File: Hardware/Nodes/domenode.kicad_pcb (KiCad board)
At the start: 2 copper layers, 100 x 65 mm, 9 parts, among them J10 CAN_BOARD, J12 RGB_SHIELD, J13 RGB_SHIELD, J15 CAN_IN, J16 CAN_OUT, U1 MINI-360, U2 AMS1117-3.3, U4 SN65HVD230, U5 ESP32-WROOM

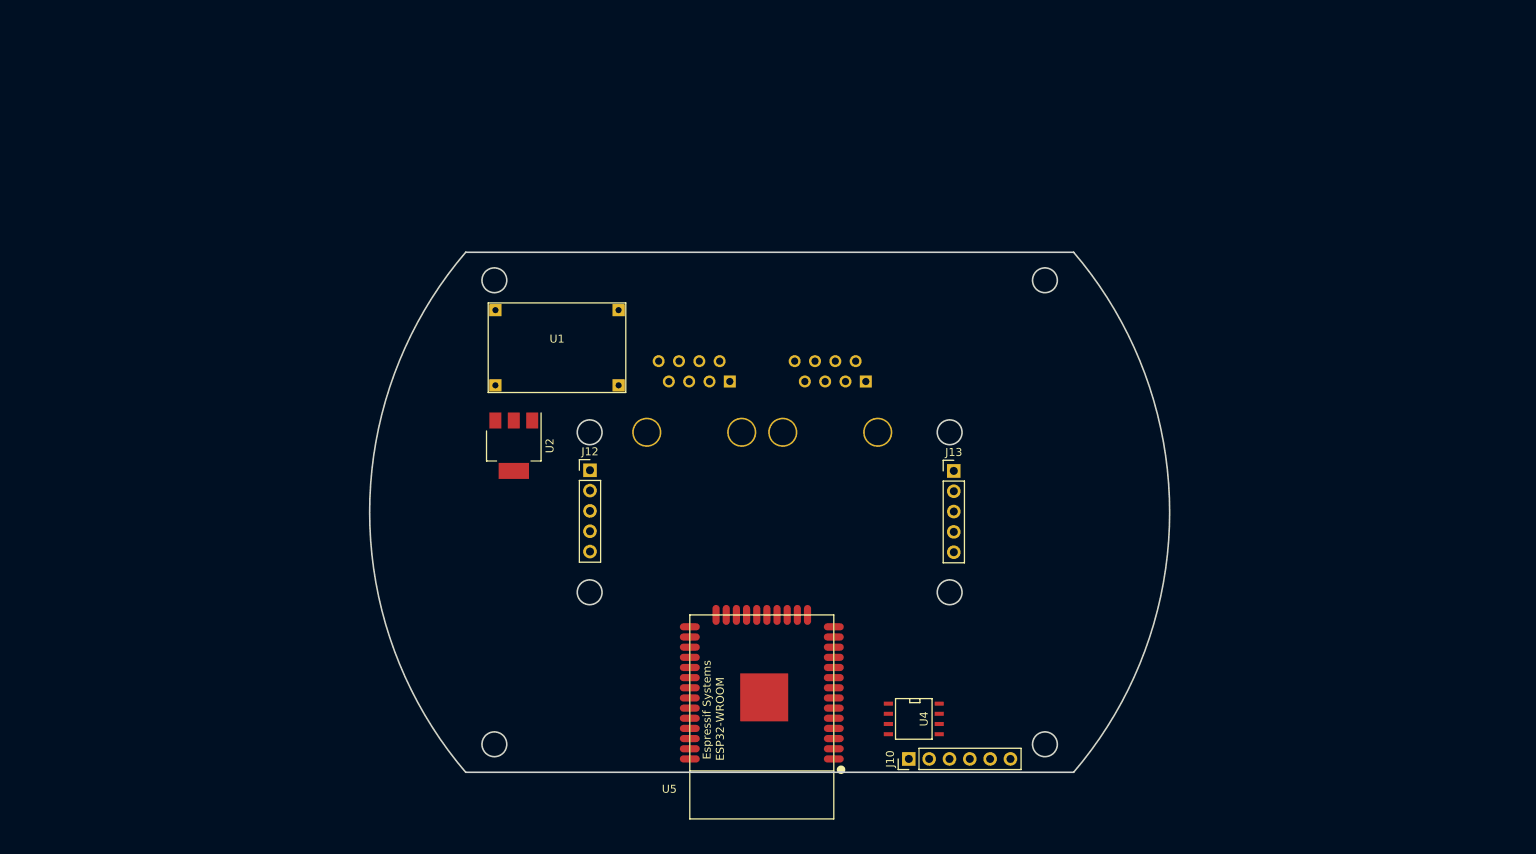
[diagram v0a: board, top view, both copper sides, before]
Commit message: More footprint assigns. More PCB design.
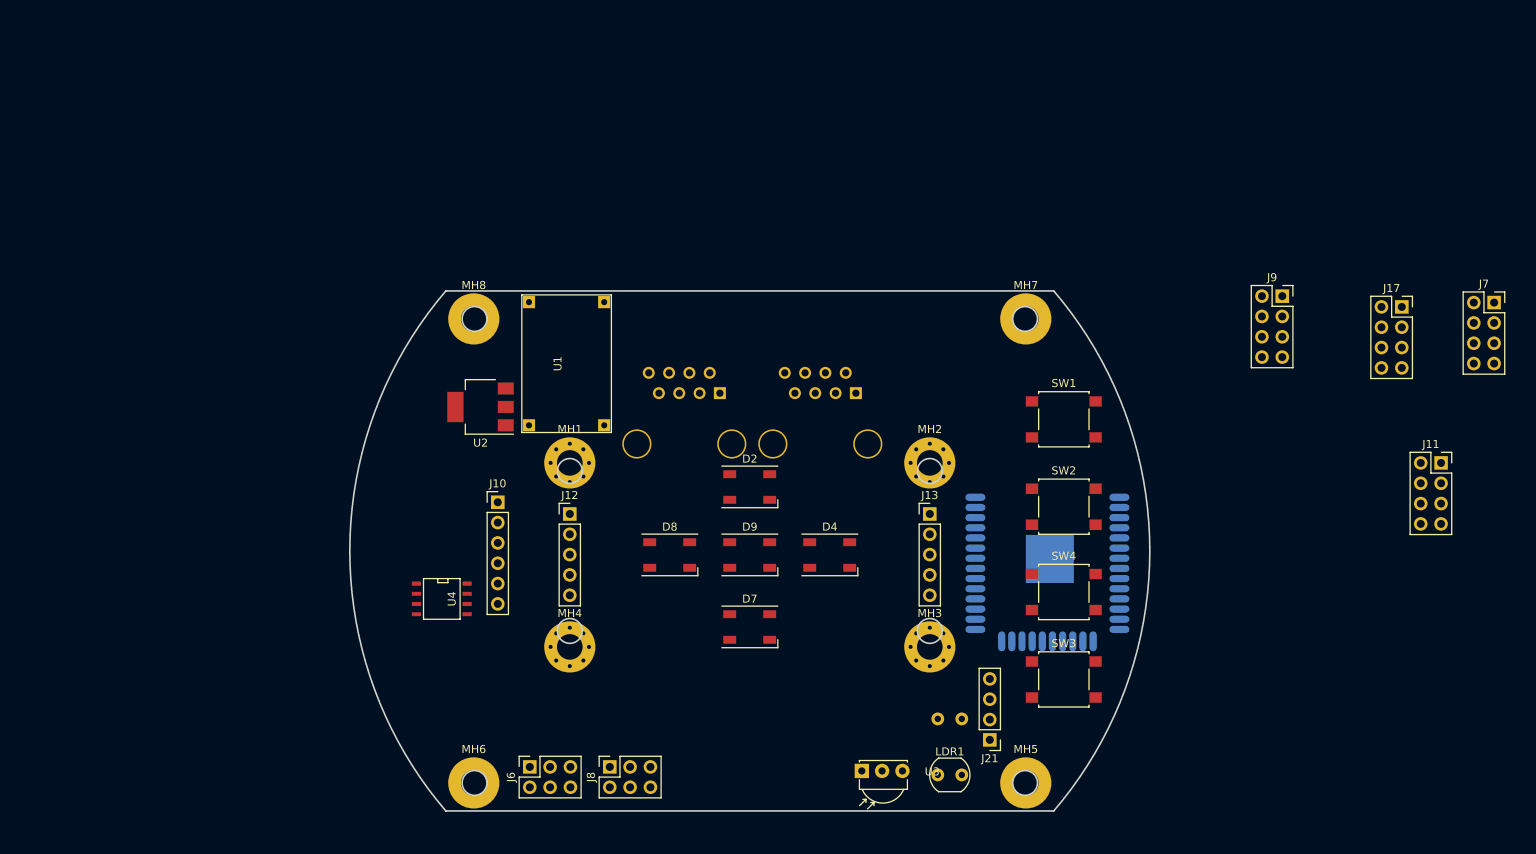
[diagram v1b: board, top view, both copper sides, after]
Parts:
- added D2: WS2812B, LEDs:LED_WS2812B-PLCC4, F.Cu at (148.5, 97.0)
- added D4: WS2812B, LEDs:LED_WS2812B-PLCC4, F.Cu at (158.5, 105.5)
- added D7: WS2812B, LEDs:LED_WS2812B-PLCC4, F.Cu at (148.5, 114.5)
- added D8: WS2812B, LEDs:LED_WS2812B-PLCC4, F.Cu at (138.5, 105.5)
- added D9: WS2812B, LEDs:LED_WS2812B-PLCC4, F.Cu at (148.5, 105.5)
- added J11: CANV, Socket_Strips:Socket_Strip_Straight_2x04_Pitch2.54mm, F.Cu at (234.9, 94.0)
- added J17: SWITCHES, Socket_Strips:Socket_Strip_Straight_2x04_Pitch2.54mm, F.Cu at (230.0, 74.5)
- added J21: GROVE/I2C, Socket_Strips:Socket_Strip_Straight_1x04_Pitch2.54mm, F.Cu at (178.5, 128.6)
- added J6: SENSOR, Socket_Strips:Socket_Strip_Straight_2x03_Pitch2.54mm, F.Cu at (121.0, 132.0)
- added J7: 3V3, Socket_Strips:Socket_Strip_Straight_2x04_Pitch2.54mm, F.Cu at (241.5, 74.0)
- added J8: TOUCH, Socket_Strips:Socket_Strip_Straight_2x03_Pitch2.54mm, F.Cu at (131.0, 132.0)
- added J9: 5V, Socket_Strips:Socket_Strip_Straight_2x04_Pitch2.54mm, F.Cu at (215.1, 73.2)
- added LDR1: FLDR, Opto-Devices:Resistor_LDR_5x4.1_RM3, F.Cu at (172.0, 133.0)
- added LDR2: RLDR, Opto-Devices:Resistor_LDR_5x4.1_RM3, B.Cu at (172.0, 126.0)
- added MH1: GND, Mounting_Holes:MountingHole_3.2mm_M3_Pad_Via, F.Cu at (126.0, 94.0)
- added MH2: GND, Mounting_Holes:MountingHole_3.2mm_M3_Pad_Via, F.Cu at (171.0, 94.0)
- added MH3: GND, Mounting_Holes:MountingHole_3.2mm_M3_Pad_Via, F.Cu at (171.0, 117.0)
- added MH4: GND, Mounting_Holes:MountingHole_3.2mm_M3_Pad_Via, F.Cu at (126.0, 117.0)
- added MH5: TOUCH5, Mounting_Holes:MountingHole_3.2mm_M3_Pad, F.Cu at (183.0, 134.0)
- added MH6: TOUCH5, Mounting_Holes:MountingHole_3.2mm_M3_Pad, F.Cu at (114.0, 134.0)
- added MH7: TOUCH5, Mounting_Holes:MountingHole_3.2mm_M3_Pad, F.Cu at (183.0, 76.0)
- added MH8: TOUCH5, Mounting_Holes:MountingHole_3.2mm_M3_Pad, F.Cu at (114.0, 76.0)
- added SW1: SW1, Buttons_Switches_SMD:SW_SPST_B3S-1000, F.Cu at (187.8, 88.5)
- added SW2: SW2, Buttons_Switches_SMD:SW_SPST_B3S-1000, F.Cu at (187.8, 99.5)
- added SW3: RESET, Buttons_Switches_SMD:SW_SPST_B3S-1000, F.Cu at (187.8, 121.1)
- added SW4: BOOT, Buttons_Switches_SMD:SW_SPST_B3S-1000, F.Cu at (187.8, 110.1)
- added U3: TSDP341xx, Opto-Devices:IRReceiver_Vishay_MOLD-3pin, F.Cu at (162.5, 132.5)
- U5: moved to B.Cu
- moved U4 60.9 mm to (110.0, 111.0)
- moved J10 60.6 mm to (117.0, 98.9), turned to 0 degrees
- moved U5 42.0 mm to (185.7, 103.5)
- moved U1 13.0 mm to (120.0, 73.0), turned to 270 degrees
- moved U2 6.38 mm to (114.8, 87.0), turned to 180 degrees
- moved J13 6.16 mm to (171.0, 100.4)
- moved J12 6.02 mm to (126.0, 100.4)
- moved J15 1.91 mm to (144.8, 85.3)
- moved J16 1.91 mm to (161.8, 85.3)
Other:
- outline, holes or cut-outs redrawn

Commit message: Bit more layout :)
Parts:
- U5: moved to F.Cu
- moved J9 106.8 mm to (110.0, 92.5), turned to 90 degrees
- moved J11 102.1 mm to (133.2, 84.2), turned to 90 degrees
- moved J17 64.2 mm to (166.5, 84.0), turned to 90 degrees
- moved J7 55.8 mm to (187.1, 86.5), turned to 270 degrees
- moved SW1 49.1 mm to (140.0, 77.0)
- moved SW3 46.6 mm to (172.5, 77.0)
- moved SW2 43.1 mm to (151.0, 77.0)
- moved SW4 42.3 mm to (161.5, 77.0)
- moved D2 10.0 mm to (148.5, 87.0), turned to 90 degrees
- moved D7 8.50 mm to (148.5, 123.0), turned to 90 degrees
- moved D4 8.02 mm to (166.5, 105.0), turned to 180 degrees
- moved D8 8.02 mm to (130.5, 105.0)
- moved J15 7.61 mm to (143.5, 92.8)
- moved J16 7.54 mm to (162.5, 92.8)
- moved J12 1.00 mm to (125.0, 100.4)
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
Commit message: Populated board and footprints.
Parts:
- removed J8: TOUCH, Socket_Strips:Socket_Strip_Straight_2x03_Pitch2.54mm
- removed U4: SN65HVD230, SMD_Packages:SOIC-8-N
- added C1: 10uF, Capacitor_SMD:C_0603_1608Metric_Pad1.05x0.95mm_HandSolder, F.Cu at (140.8, 52.5)
- added C10: 100nF, Capacitor_SMD:C_0603_1608Metric_Pad1.05x0.95mm_HandSolder, F.Cu at (140.8, 51.0)
- added C11: 100nF, Capacitor_SMD:C_0603_1608Metric_Pad1.05x0.95mm_HandSolder, F.Cu at (137.4, 54.0)
- added C12: 100nF, Capacitor_SMD:C_0603_1608Metric_Pad1.05x0.95mm_HandSolder, F.Cu at (123.8, 56.8)
- added C13: 100nF, Capacitor_SMD:C_0603_1608Metric_Pad1.05x0.95mm_HandSolder, F.Cu at (137.4, 55.5)
- added C2: 10uF, Capacitor_SMD:C_0603_1608Metric_Pad1.05x0.95mm_HandSolder, F.Cu at (127.1, 56.8)
- added C3: 100uF, Capacitor_SMD:CP_Elec_4x3.9, F.Cu at (128.7, 53.6)
- added C4: 10uF, Capacitor_SMD:C_0603_1608Metric_Pad1.05x0.95mm_HandSolder, F.Cu at (138.4, 49.5)
- added C5: 10uF, Capacitor_SMD:C_0603_1608Metric_Pad1.05x0.95mm_HandSolder, F.Cu at (130.5, 56.8)
- added C6: 100nF, Capacitor_SMD:C_0603_1608Metric_Pad1.05x0.95mm_HandSolder, F.Cu at (137.4, 51.0)
- added C7: 100nF, Capacitor_SMD:C_0603_1608Metric_Pad1.05x0.95mm_HandSolder, F.Cu at (137.4, 52.5)
- added C8: 100nF, Capacitor_SMD:C_0603_1608Metric_Pad1.05x0.95mm_HandSolder, F.Cu at (133.8, 55.8)
- added C9: 100nF, Capacitor_SMD:C_0603_1608Metric_Pad1.05x0.95mm_HandSolder, F.Cu at (152.5, 59.0)
- added D1: WS2812B, LED_SMD:LED_WS2812B_PLCC4_5.0x5.0mm_P3.2mm, F.Cu at (148.5, 87.0)
- added D10: 1N5819, Diode_SMD:D_0603_1608Metric_Pad1.05x0.95mm_HandSolder, F.Cu at (136.6, 83.0)
- added D11: POWER, LED_SMD:LED_0805_2012Metric_Pad1.15x1.40mm_HandSolder, F.Cu at (109.0, 80.0)
- added D12: BLINK, LED_SMD:LED_0805_2012Metric_Pad1.15x1.40mm_HandSolder, F.Cu at (188.0, 80.0)
- added D13: IRLED, LED_THT:LED_D3.0mm_IRBlack, F.Cu at (113.0, 124.5)
- added D3: WS2812B, LED_SMD:LED_WS2812B_PLCC4_5.0x5.0mm_P3.2mm, F.Cu at (148.5, 123.0)
- added D5: WS2812B, LED_SMD:LED_WS2812B_PLCC4_5.0x5.0mm_P3.2mm, F.Cu at (138.5, 98.5)
- added D6: WS2812B, LED_SMD:LED_WS2812B_PLCC4_5.0x5.0mm_P3.2mm, F.Cu at (158.5, 98.5)
- added J1: MIC_JUMPER, Connector_PinHeader_2.54mm:PinHeader_1x02_P2.54mm_Vertical, F.Cu at (133.5, 41.5)
- added J14: CANV, Connector_PinHeader_2.54mm:PinHeader_2x04_P2.54mm_Vertical, F.Cu at (112.5, 49.0)
- added J18: ISP, Connector_PinHeader_2.54mm:PinHeader_1x04_P2.54mm_Vertical, F.Cu at (189.5, 123.0)
- added J19: CAN_IN, Connector_RJ:RJ45_Amphenol_RJHSE5380, B.Cu at (155.0, 93.5)
- added J2: MIC_HEADER, Connector_PinHeader_2.54mm:PinHeader_1x03_P2.54mm_Vertical, F.Cu at (127.2, 44.3)
- added J20: CAN_OUT, Connector_RJ:RJ45_Amphenol_RJHSE5380, B.Cu at (135.0, 93.5)
- added J3: SW0, Connector_PinHeader_2.54mm:PinHeader_1x02_P2.54mm_Vertical, F.Cu at (184.5, 127.0)
- added U6: SN65HVD230, Package_SO:SOIC-8_3.9x4.9mm_P1.27mm, F.Cu at (181.0, 84.0)
- D2, D4, D7, D8, D9: footprint LEDs:LED_WS2812B-PLCC4 -> LED_SMD:LED_WS2812B_PLCC4_5.0x5.0mm_P3.2mm
- J10: value CAN_BOARD -> 3V3; footprint Socket_Strips:Socket_Strip_Straight_1x06_Pitch2.54mm -> Connector_PinHeader_2.54mm:PinHeader_2x04_P2.54mm_Vertical
- J11: value CANV -> TOUCH; footprint Socket_Strips:Socket_Strip_Straight_2x04_Pitch2.54mm -> Connector_PinHeader_2.54mm:PinHeader_2x03_P2.54mm_Vertical
- J12: value RGB_SHIELD -> 5V; footprint Socket_Strips:Socket_Strip_Straight_1x05_Pitch2.54mm -> Connector_PinHeader_2.54mm:PinHeader_2x04_P2.54mm_Vertical
- J13: value RGB_SHIELD -> CAN_BOARD; footprint Socket_Strips:Socket_Strip_Straight_1x05_Pitch2.54mm -> Connector_PinSocket_2.54mm:PinSocket_1x06_P2.54mm_Vertical
- J15: value CAN_IN -> RGB_SHIELD; footprint Connectors:RJ45_8 -> Connector_PinSocket_2.54mm:PinSocket_1x05_P2.54mm_Vertical; moved to F.Cu
- J16: value CAN_OUT -> RGB_SHIELD; footprint Connectors:RJ45_8 -> Connector_PinSocket_2.54mm:PinSocket_1x05_P2.54mm_Vertical; moved to F.Cu
- J17: value SWITCHES -> GROVE/I2C; footprint Socket_Strips:Socket_Strip_Straight_2x04_Pitch2.54mm -> Connector_PinHeader_2.54mm:PinHeader_1x04_P2.54mm_Vertical
- J21: value GROVE/I2C -> SWITCHES; footprint Socket_Strips:Socket_Strip_Straight_1x04_Pitch2.54mm -> Connector_PinHeader_2.54mm:PinHeader_2x04_P2.54mm_Vertical
- J6: value SENSOR -> POWER_TEST; footprint Socket_Strips:Socket_Strip_Straight_2x03_Pitch2.54mm -> Connector_PinHeader_2.54mm:PinHeader_1x04_P2.54mm_Vertical
- J7: value 3V3 -> SPEAKER; footprint Socket_Strips:Socket_Strip_Straight_2x04_Pitch2.54mm -> Connector_PinHeader_2.54mm:PinHeader_1x02_P2.54mm_Vertical
- J9: value 5V -> SENSOR; footprint Socket_Strips:Socket_Strip_Straight_2x04_Pitch2.54mm -> Connector_PinHeader_2.54mm:PinHeader_2x03_P2.54mm_Vertical
- MH1, MH2, MH3, MH4: footprint Mounting_Holes:MountingHole_3.2mm_M3_Pad_Via -> MountingHole:MountingHole_3.2mm_M3_Pad
- MH5, MH6, MH7, MH8: footprint Mounting_Holes:MountingHole_3.2mm_M3_Pad -> MountingHole:MountingHole_3.2mm_M3_Pad
- U2: footprint TO_SOT_Packages_SMD:SOT-223-3_TabPin2 -> Package_TO_SOT_SMD:SOT-223-3_TabPin2
- U3: value TSDP341xx -> ESP32-WROOM; footprint Opto-Devices:IRReceiver_Vishay_MOLD-3pin -> ESP32-footprints-Lib:ESP32-WROOM
- U5: value ESP32-WROOM -> TSDP341xx; footprint ESP32-footprints-Lib:ESP32-WROOM -> OptoDevice:Vishay_MOLD-3Pin
- moved U5 83.1 mm to (105.0, 124.0), turned to 0 degrees
- moved J11 51.8 mm to (120.5, 134.5)
- moved J9 47.2 mm to (131.5, 134.5)
- moved J6 41.8 mm to (106.0, 93.0), turned to 180 degrees
- moved J16 38.7 mm to (124.5, 100.0), turned to 0 degrees
- moved U3 37.0 mm to (185.5, 103.5), turned to 180 degrees
- moved J21 36.5 mm to (142.5, 134.5), turned to 90 degrees
- moved D4 36.0 mm to (130.5, 105.0), turned to 90 degrees
- moved J12 35.1 mm to (90.0, 102.5), turned to 270 degrees
- moved J15 29.9 mm to (172.5, 100.0), turned to 0 degrees
- moved D2 25.5 mm to (166.5, 105.0)
- moved U1 15.5 mm to (134.5, 78.5), turned to 180 degrees
- moved D7 15.2 mm to (158.5, 111.5)
- moved J13 14.2 mm to (179.0, 88.0), turned to 90 degrees
- moved J7 13.2 mm to (174.0, 88.0)
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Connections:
- D4 pad 4: Net-(D2-Pad2) -> Net-(D3-Pad2)
- D7 pad 4: Net-(D4-Pad2) -> CANGND
- J10 pad 3: CTX -> VCC
- J10 pad 4: CRX -> CANGND
- J10 pad 5: CANH -> VCC
- J10 pad 6: CANL -> CANGND
- J11 pad 1: +24V -> TOUCH5
- J11 pad 2: CANGND -> TOUCH3
- J11 pad 3: +24V -> VCC
- J11 pad 4: CANGND -> VCC
- J11 pad 5: +24V -> CANGND
- J12 pad 1: +24V -> +5V
- J12 pad 2: RED -> CANGND
- J12 pad 3: GREEN -> +5V
- J12 pad 4: BLUE -> CANGND
- J12 pad 5: CANGND -> +5V
- J13 pad 1: +24V -> VCC
- J13 pad 2: RED -> CANGND
- J13 pad 3: GREEN -> CTX
- J13 pad 4: BLUE -> CRX
- J13 pad 5: CANGND -> CANH
- J15 pad 1: CANV -> +24V
- J15 pad 2: CANV -> RED
- J15 pad 3: CANV -> GREEN
- J15 pad 4: CANGND -> BLUE
- J16 pad 1: CANV -> +24V
- J16 pad 2: CANV -> RED
- J16 pad 3: CANV -> GREEN
- J16 pad 4: CANGND -> BLUE
- J17 pad 1: SW1 -> SCL
- J17 pad 2: CANGND -> SDA
- J17 pad 3: SW2 -> VCC
- J21 pad 1: SCL -> SW1
- J21 pad 2: SDA -> CANGND
- J21 pad 3: VCC -> SW2
- J6 pad 1: VP -> CANV
- J6 pad 2: VN -> +5V
- J6 pad 4: VCC -> CANGND
- J7 pad 1: VCC -> SPEAKER
- J9 pad 1: +5V -> VP
- J9 pad 2: CANGND -> VN
- J9 pad 3: +5V -> VCC
- J9 pad 4: CANGND -> VCC
- J9 pad 5: +5V -> CANGND
- U3 pad 1: IR_RX -> CANGND
- U3 pad 2: CANGND -> VCC
- U3 pad 3: VCC -> EN
- U5 pad 1: CANGND -> IR_RX
- U5 pad 2: VCC -> CANGND
- U5 pad 3: EN -> VCC

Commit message: Added SHM label somewhere on the PCB
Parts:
- added shm_logo_small: , shm_logo:shm_logo, B.Cu at (160.5, 104.5)
